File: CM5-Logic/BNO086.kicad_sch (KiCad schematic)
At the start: 2 parts, among them J18 6130XX11821_61300811821, J19 6130XX11821_61300811821

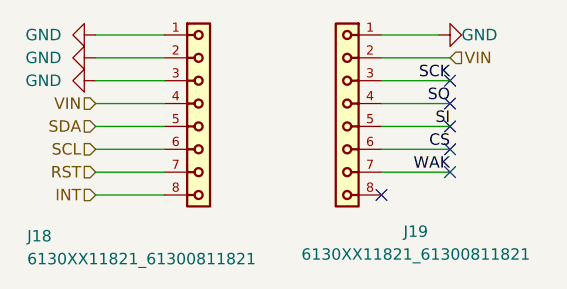
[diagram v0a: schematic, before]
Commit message: changes USB port, adds TMC2209 SilentStepStick footprint, redoes PCB Layout
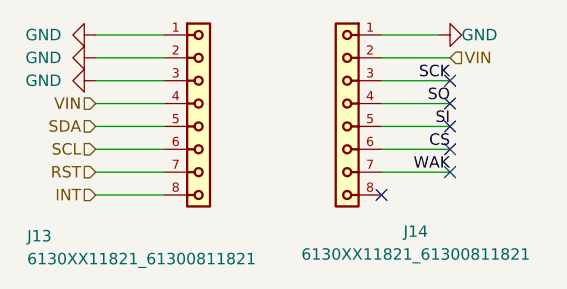
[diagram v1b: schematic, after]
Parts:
- renumbered J18 to J13, J19 to J14
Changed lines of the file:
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@@
 		(on_board yes)
 		(dnp no)
-		(property "Reference" "J19"
+		(property "Reference" "J14"
 			(at 120.65 84.074 90)
 			(effects
@@
 			(project ""
 				(path "/e63e39d7-6ac0-4ffd-8aa3-1841a4541b55/e34db096-2f2b-46af-8af2-078f818cdd39"
-					(reference "J19")
+					(reference "J14")
 					(unit 1)
 				)
@@
 		(dnp no)
 		(fields_autoplaced yes)
-		(property "Reference" "#PWR059"
+		(property "Reference" "#PWR058"
 			(at 78.74 64.77 0)
 			(effects
@@
 			(project ""
 				(path "/e63e39d7-6ac0-4ffd-8aa3-1841a4541b55/e34db096-2f2b-46af-8af2-078f818cdd39"
-					(reference "#PWR059")
+					(reference "#PWR058")
 					(unit 1)
 				)
@@
 		(dnp no)
 		(fields_autoplaced yes)
-		(property "Reference" "#PWR058"
+		(property "Reference" "#PWR057"
 			(at 78.74 62.23 0)
 			(effects
@@
 			(project ""
 				(path "/e63e39d7-6ac0-4ffd-8aa3-1841a4541b55/e34db096-2f2b-46af-8af2-078f818cdd39"
-					(reference "#PWR058")
+					(reference "#PWR057")
 					(unit 1)
 				)
@@
 		(on_board yes)
 		(dnp no)
-		(property "Reference" "#PWR061"
+		(property "Reference" "#PWR060"
 			(at 129.54 62.23 0)
 			(effects
@@
 			(project ""
 				(path "/e63e39d7-6ac0-4ffd-8aa3-1841a4541b55/e34db096-2f2b-46af-8af2-078f818cdd39"
-					(reference "#PWR061")
+					(reference "#PWR060")
 					(unit 1)
 				)
@@
 		(on_board yes)
 		(dnp no)
-		(property "Reference" "J18"
+		(property "Reference" "J13"
 			(at 77.47 84.582 90)
 			(effects
@@
 			(project ""
 				(path "/e63e39d7-6ac0-4ffd-8aa3-1841a4541b55/e34db096-2f2b-46af-8af2-078f818cdd39"
-					(reference "J18")
+					(reference "J13")
 					(unit 1)
 				)
@@
 		(dnp no)
 		(fields_autoplaced yes)
-		(property "Reference" "#PWR060"
+		(property "Reference" "#PWR059"
 			(at 78.74 67.31 0)
 			(effects
@@
 			(project ""
 				(path "/e63e39d7-6ac0-4ffd-8aa3-1841a4541b55/e34db096-2f2b-46af-8af2-078f818cdd39"
-					(reference "#PWR060")
-					(unit 1)
-				)
+					(reference "#PWR059")
+					(unit 1)
+				)
